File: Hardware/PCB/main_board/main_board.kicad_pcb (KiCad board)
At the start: 2 copper layers, 170 x 170 mm, 88 parts, among them J1 SWD, J2 USB_A, J3 DIN-5_180degree, J4 USB_B, J5 Conn_Coaxial, J6 AudioJack3, Q1 BC547, U1 MCP6002-xSN, U2 NUCLEO-F446RE, U3 6N137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

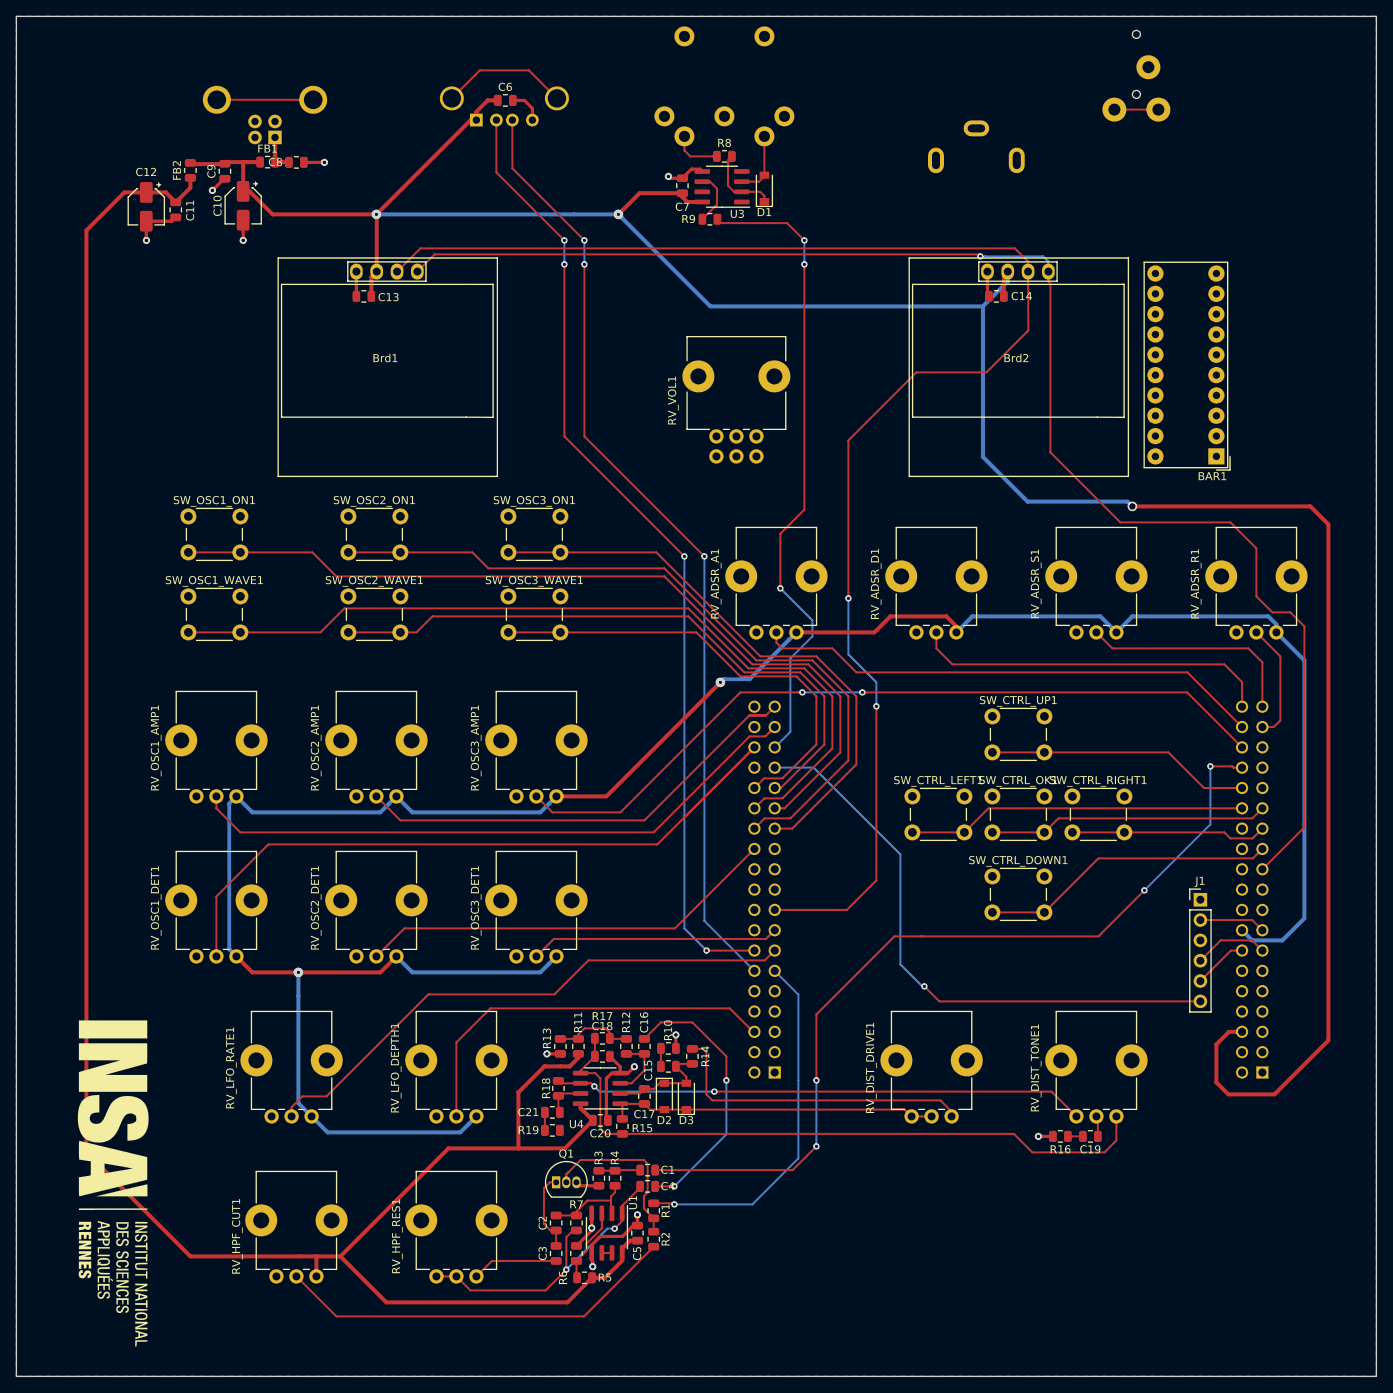
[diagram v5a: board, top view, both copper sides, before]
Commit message: Cleanup routing
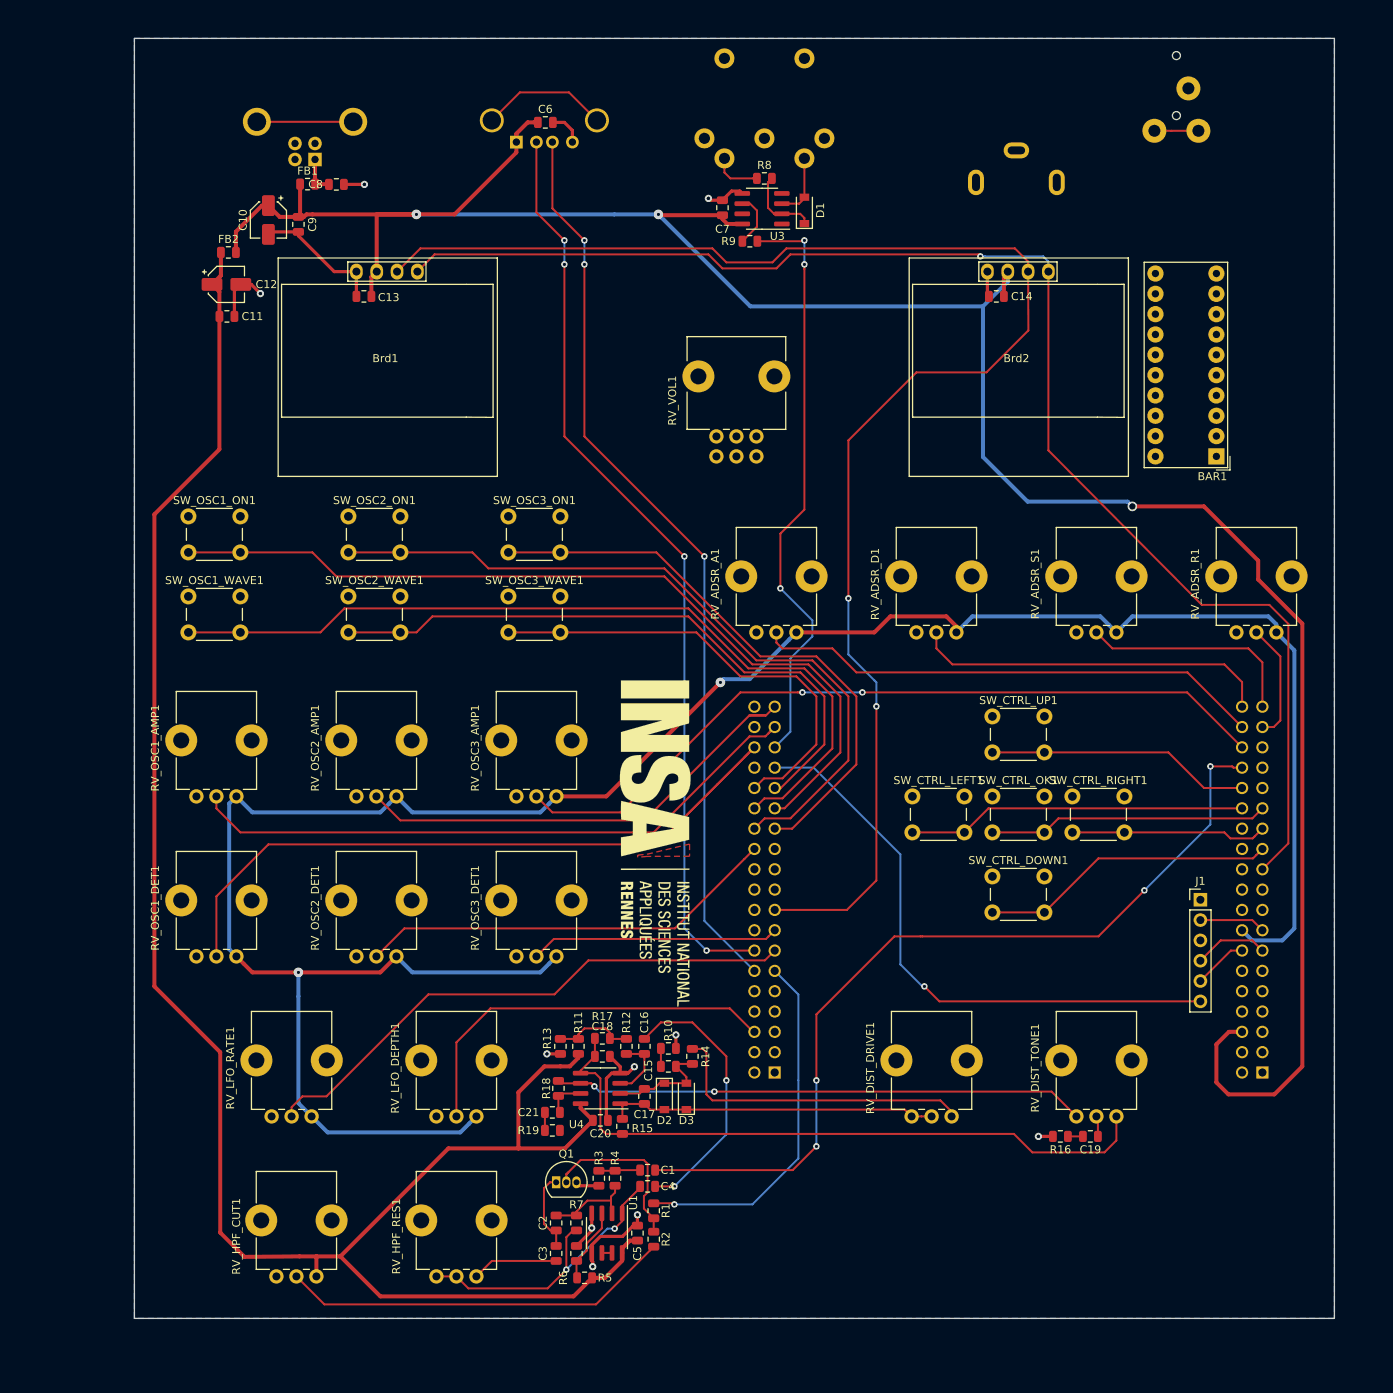
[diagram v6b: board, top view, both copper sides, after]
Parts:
- moved G*** 80.0 mm to (100.5, 160.5)
- moved C11 14.8 mm to (46.6, 94.8), turned to 0 degrees
- moved C12 13.9 mm to (46.5, 90.8), turned to 0 degrees
- moved C9 11.3 mm to (55.5, 83.2)
- moved FB2 11.3 mm to (46.8, 86.8), turned to 0 degrees
- moved C6 5.71 mm to (86.4, 70.5)
- moved C7 5.71 mm to (108.5, 81.2)
- moved C8 5.71 mm to (60.2, 78.2)
- moved D1 5.71 mm to (118.8, 81.5)
- moved FB1 5.71 mm to (56.6, 78.2)
- moved J2 5.71 mm to (82.8, 73.0)
- moved J3 5.71 mm to (113.8, 69.5)
- moved J4 5.71 mm to (57.6, 75.1)
- moved J5 5.71 mm to (145.2, 74.0)
- moved R8 5.71 mm to (113.8, 77.5)
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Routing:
- net +5VA: track 274.2 -> 250.0 mm
- net +5V: track 322.8 -> 309.6 mm
- net GND: track 64.7 -> 74.4 mm, vias 12 -> 10
- net /MIDI/MIDI_Serial_RX: track 80.2 -> 74.1 mm
- net /MIDI/MIDI_USB_D-: track 120.7 -> 115.9 mm
- net /MIDI/MIDI_USB_D+: track 118.9 -> 114.1 mm
- net /HMI/I2C_display_SDA: track 180.9 -> 176.2 mm
- net /HMI/I2C_display_SCL: track 188.2 -> 189.7 mm
- net Net-(R2-Pad2): track 50.3 -> 49.1 mm
- net +3V3: track 299.5 -> 298.4 mm
- added copper zone on F.Cu, net (none)
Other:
- board size 170 x 170 mm -> 150 x 160 mm

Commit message: Change GPIO config
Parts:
- moved C6 6.00 mm to (86.4, 76.5)
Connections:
- SW_OSC1_WAVE1 pad 2: /MCU/GPIO_PB14 -> /MCU/GPIO_PB8
- SW_OSC2_ON1 pad 2: /MCU/GPIO_PB15 -> /MCU/GPIO_PB9
- U2 pad CN10_26: /MCU/GPIO_PB15 -> /power/USB_B_D+
- U2 pad CN10_28: /MCU/GPIO_PB14 -> /power/USB_B_D-
- U2 pad CN10_3: Net-(U2-PadCN10_3) -> /MCU/GPIO_PB8
- U2 pad CN10_5: Net-(U2-PadCN10_5) -> /MCU/GPIO_PB9
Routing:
- net /power/USB_B_D+: track 0.00 -> 152.9 mm, vias 0 -> 1
- net /power/USB_B_D-: track 0.00 -> 148.2 mm, vias 0 -> 1
- net /MCU/GPIO_PB8: track 0.00 -> 118.3 mm, vias 0 -> 1
- net /MCU/GPIO_PB9: track 0.00 -> 105.9 mm, vias 0 -> 1
- net /MCU/GPIO_PB14: track 105.7 -> 0.00 mm
- net /MCU/GPIO_PB15: track 93.2 -> 0.00 mm
- net /MIDI/MIDI_USB_D+: track 114.1 -> 128.4 mm, vias 3 -> 0
- net /MIDI/MIDI_USB_D-: track 115.9 -> 129.8 mm, vias 4 -> 0
- net +5V: track 309.6 -> 319.2 mm, vias 3 -> 2
- net Net-(J2-Pad5): track 16.0 -> 13.1 mm

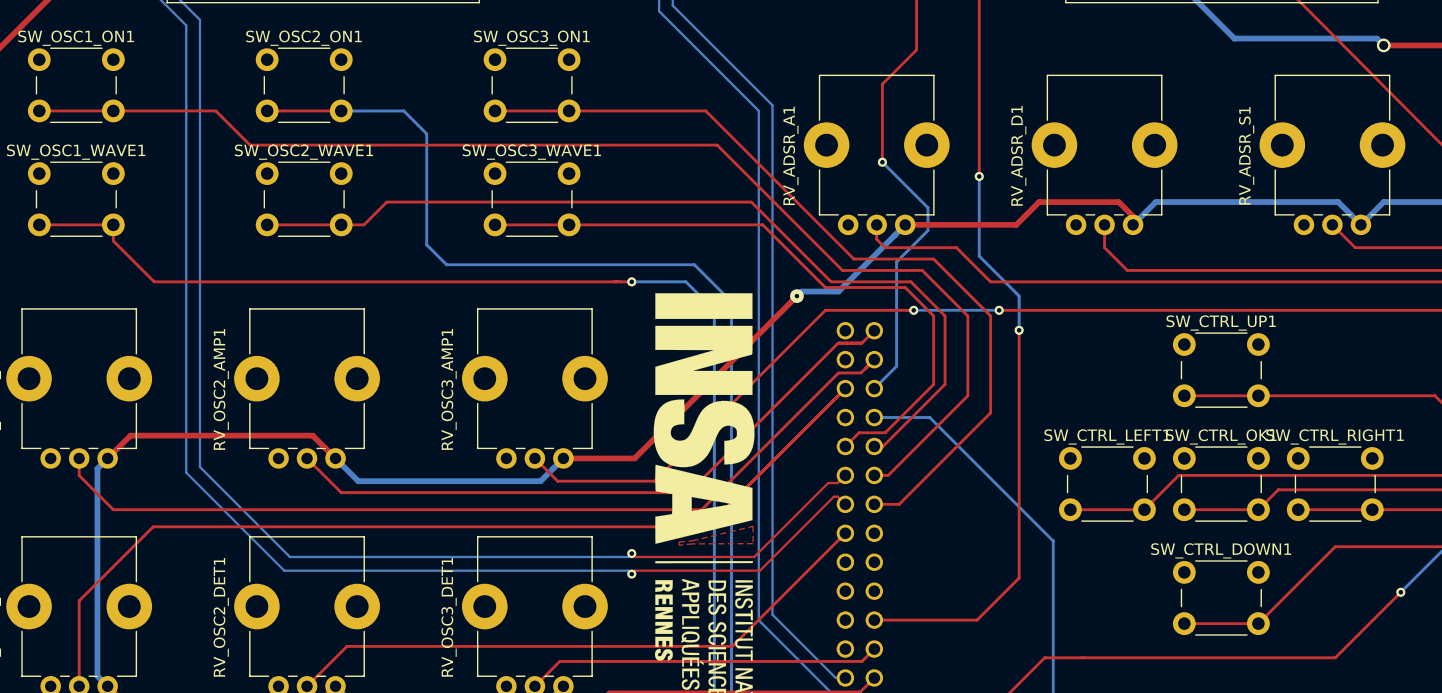
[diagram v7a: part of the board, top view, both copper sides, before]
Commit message: Add debounce capacitors
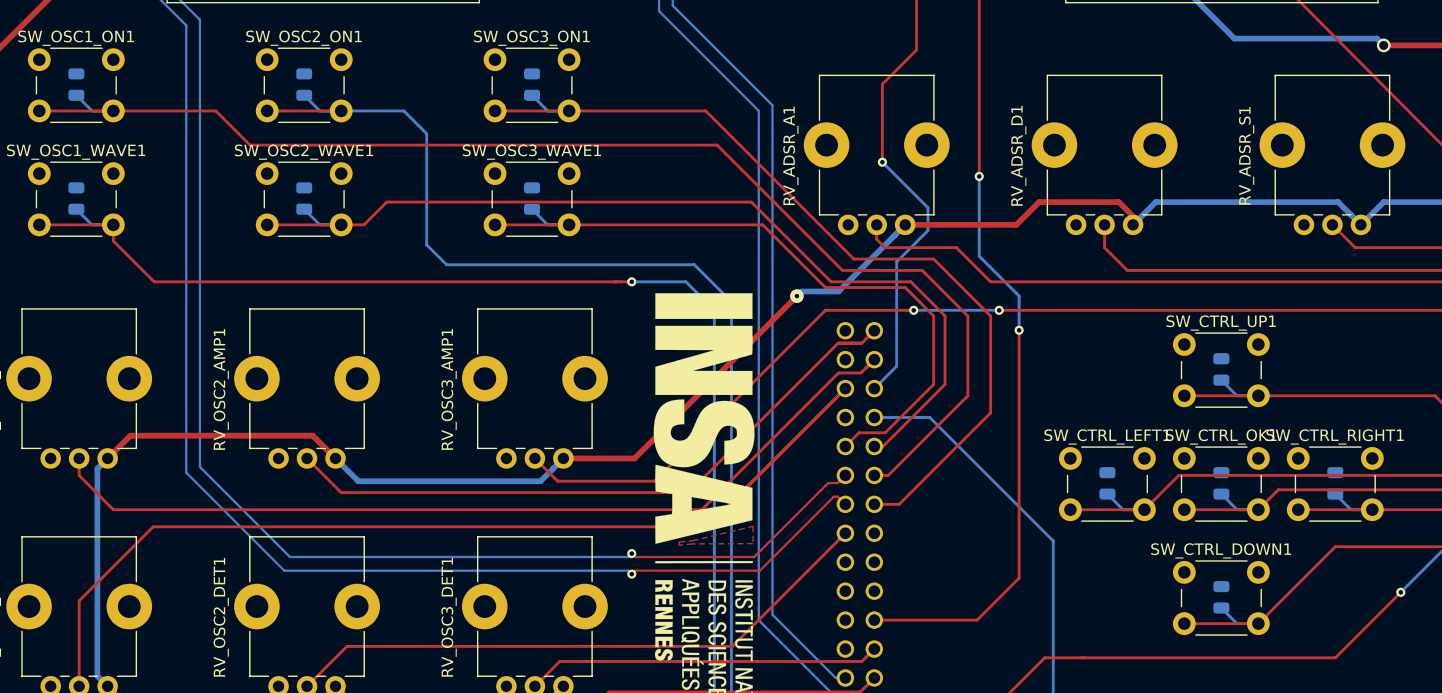
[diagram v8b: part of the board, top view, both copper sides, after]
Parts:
- added C22: 100n, Capacitor_SMD:C_0805_2012Metric, B.Cu at (135.5, 156.9)
- added C23: 100n, Capacitor_SMD:C_0805_2012Metric, B.Cu at (155.5, 156.9)
- added C24: 100n, Capacitor_SMD:C_0805_2012Metric, B.Cu at (145.5, 146.9)
- added C25: 100n, Capacitor_SMD:C_0805_2012Metric, B.Cu at (145.5, 166.9)
- added C26: 100n, Capacitor_SMD:C_0805_2012Metric, B.Cu at (145.5, 156.9)
- added C27: 100n, Capacitor_SMD:C_0805_2012Metric, B.Cu at (45.0, 121.9)
- added C28: 100n, Capacitor_SMD:C_0805_2012Metric, B.Cu at (65.0, 121.9)
- added C29: 100n, Capacitor_SMD:C_0805_2012Metric, B.Cu at (85.0, 121.9)
- added C30: 100n, Capacitor_SMD:C_0805_2012Metric, B.Cu at (45.0, 131.9)
- added C31: 100n, Capacitor_SMD:C_0805_2012Metric, B.Cu at (65.0, 131.9)
- added C32: 100n, Capacitor_SMD:C_0805_2012Metric, B.Cu at (85.0, 131.9)
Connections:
- net /MCU/GPIO_PC15 renamed /HMI/CTRL_OK
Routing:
- net /MCU/GPIO_PB9: track 105.9 -> 109.7 mm
- net /MCU/GPIO_PB5: track 79.0 -> 82.8 mm
- net /MCU/GPIO_PB4: track 107.1 -> 110.9 mm
- net /MCU/GPIO_PB13: track 57.8 -> 61.6 mm
- net /MCU/GPIO_PB10: track 73.0 -> 76.8 mm
- net /HMI/CTRL_UP: track 33.1 -> 36.9 mm
- net /HMI/CTRL_RIGHT: track 24.6 -> 28.4 mm
- net /HMI/CTRL_OK: track 35.0 -> 38.8 mm
- net /HMI/CTRL_LEFT: track 42.5 -> 46.3 mm
- net /HMI/CTRL_DOWN: track 37.0 -> 40.9 mm
- net /MCU/GPIO_PB8: track 118.3 -> 122.1 mm
